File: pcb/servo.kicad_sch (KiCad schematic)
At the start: 1 part, among them J5 0436500315

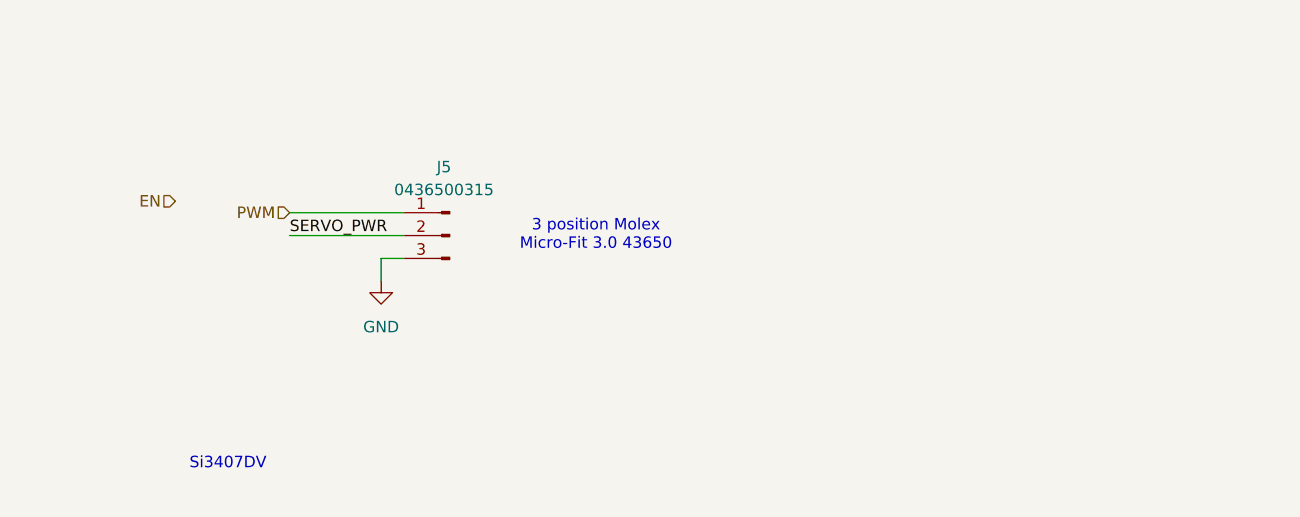
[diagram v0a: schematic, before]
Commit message: Create servo schematic
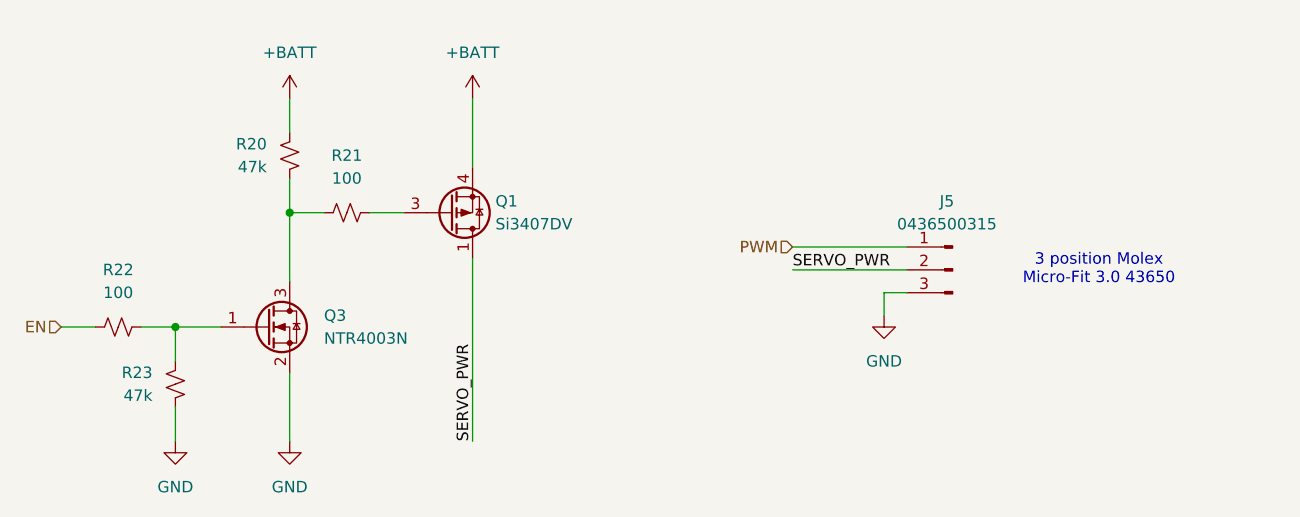
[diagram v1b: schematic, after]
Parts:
- added Q1: Si3407DV, Package_SO:TSOP-6_1.65x3.05mm_P0.95mm, symbol Vishay_FET:Si3407DV
- added Q3: NTR4003N, Package_TO_SOT_SMD:SOT-23-3, symbol Transistor_FET:Q_NMOS_GSD
- added R20, R23: 47k, symbol Device:R_Small_US
- added R21, R22: 100, symbol Device:R_Small_US
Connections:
- net EN: now also R22.1
- net GND: now also Q3.2 (S), R23.2
- net SERVO_PWR: now also Q1.1 (D), Q1.2 (D), Q1.5 (D), Q1.6 (D)
- new net: Q3.3 (D), R20.2, R21.1
- new net: Q1.3 (G), R21.2
- new net: Q3.1 (G), R22.2, R23.1
- new net +BATT: Q1.4 (S), R20.1
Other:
- note removed: "Si3407DV"
- moved on the sheet: J5

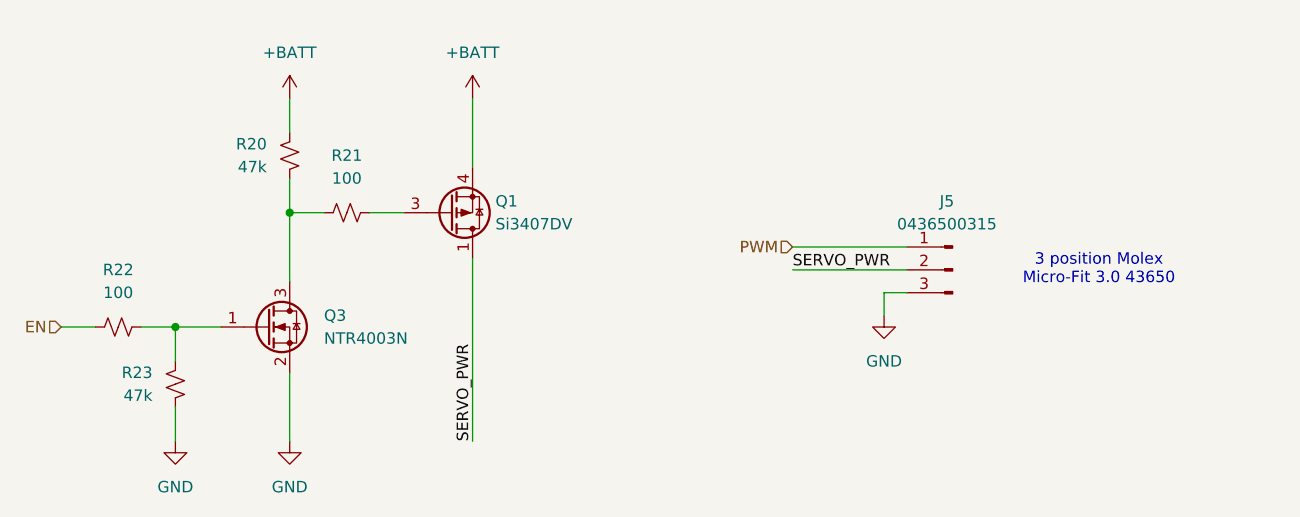
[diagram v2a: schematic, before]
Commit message: Update servo.kicad_sch
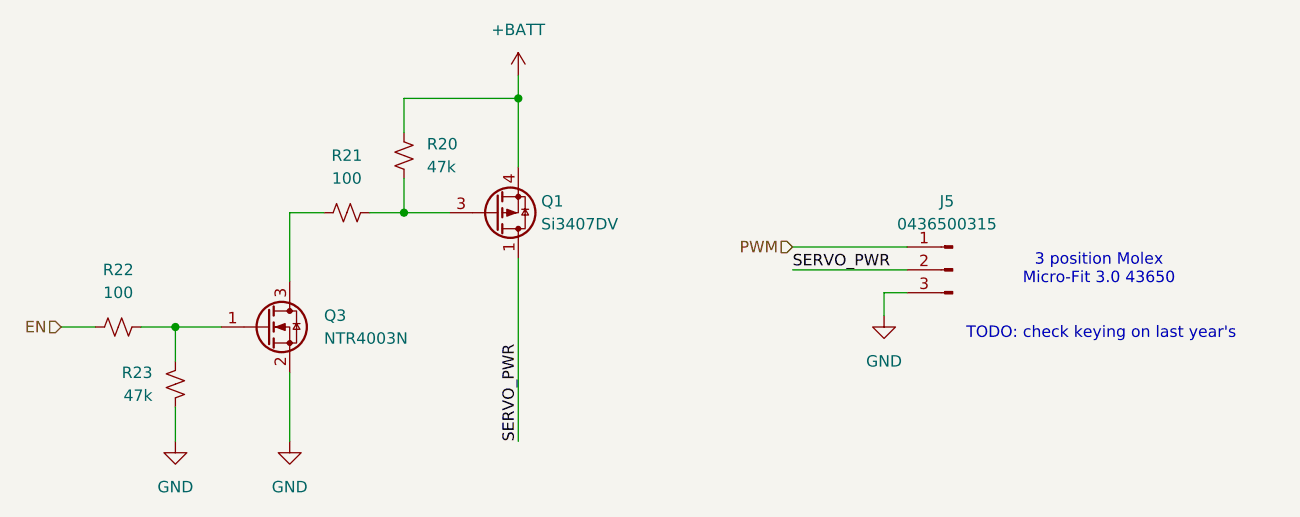
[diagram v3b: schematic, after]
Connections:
- net at Q3.3 (D), R21.1: no longer R20.2
- net at Q1.3 (G), R21.2: now also R20.2
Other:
- note added: "TODO: check keying on last year's"
- moved on the sheet: Q1, R20
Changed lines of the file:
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@@
 		)
 	)
-	(junction
-		(at 63.5 50.8)
-		(diameter 0)
-		(color 0 0 0 0)
+	(text "TODO: check keying on last year's"
+		(exclude_from_sim no)
+		(at 153.67 64.262 0)
+		(effects
+			(font
+				(size 1.27 1.27)
+			)
+		)
 	)
 	(junction
@@
 		(color 0 0 0 0)
 	)
+	(junction
+		(at 88.9 38.1)
+		(diameter 0)
+		(color 0 0 0 0)
+	)
+	(junction
+		(at 76.2 50.8)
+		(diameter 0)
+		(color 0 0 0 0)
+	)
 	(wire
 		(pts
@@
 	(wire
 		(pts
-			(xy 63.5 38.1) (xy 63.5 41.91)
+			(xy 88.9 38.1) (xy 88.9 45.72)
 		)
 		(stroke
@@
 	(wire
 		(pts
-			(xy 83.82 38.1) (xy 83.82 45.72)
+			(xy 76.2 50.8) (xy 81.28 50.8)
 		)
 		(stroke
@@
 	(wire
 		(pts
+			(xy 76.2 38.1) (xy 76.2 41.91)
+		)
+		(stroke
+			(width 0)
+			(type default)
+		)
+	)
+	(wire
+		(pts
 			(xy 129.54 59.69) (xy 132.08 59.69)
 		)
@@
 	(wire
 		(pts
+			(xy 76.2 38.1) (xy 88.9 38.1)
+		)
+		(stroke
+			(width 0)
+			(type default)
+		)
+	)
+	(wire
+		(pts
+			(xy 88.9 35.56) (xy 88.9 38.1)
+		)
+		(stroke
+			(width 0)
+			(type default)
+		)
+	)
+	(wire
+		(pts
 			(xy 63.5 50.8) (xy 67.31 50.8)
 		)
@@
 	(wire
 		(pts
-			(xy 63.5 46.99) (xy 63.5 50.8)
-		)
-		(stroke
-			(width 0)
-			(type default)
-		)
-	)
-	(wire
-		(pts
-			(xy 83.82 55.88) (xy 83.82 76.2)
+			(xy 76.2 46.99) (xy 76.2 50.8)
+		)
+		(stroke
+			(width 0)
+			(type default)
+		)
+	)
+	(wire
+		(pts
+			(xy 88.9 55.88) (xy 88.9 76.2)
 		)
 		(stroke
@@
 	)
 	(label "SERVO_PWR"
-		(at 83.82 76.2 90)
+		(at 88.9 76.2 90)
 		(effects
 			(font
@@
 	(symbol
 		(lib_id "Device:R_Small_US")
-		(at 63.5 44.45 0)
-		(mirror y)
+		(at 76.2 44.45 0)
 		(unit 1)
 		(exclude_from_sim no)
@@
 		(dnp no)
 		(property "Reference" "R20"
-			(at 60.96 43.1799 0)
+			(at 78.74 43.1799 0)
 			(effects
 				(font
@@
 		)
 		(property "Value" "47k"
-			(at 60.96 45.7199 0)
+			(at 78.74 45.7199 0)
 			(effects
 				(font
@@
 		)
 		(property "Footprint" ""
-			(at 63.5 44.45 0)
+			(at 76.2 44.45 0)
 			(effects
 				(font
@@
 		)
 		(property "Datasheet" "~"
-			(at 63.5 44.45 0)
+			(at 76.2 44.45 0)
 			(effects
 				(font
@@
 		)
 		(property "Description" "Resistor, small US symbol"
-			(at 63.5 44.45 0)
+			(at 76.2 44.45 0)
 			(effects
 				(font
@@
 	(symbol
 		(lib_id "power:+BATT")
-		(at 83.82 38.1 0)
+		(at 88.9 35.56 0)
 		(unit 1)
 		(exclude_from_sim no)
@@
 		(fields_autoplaced yes)
 		(property "Reference" "#PWR050"
-			(at 83.82 41.91 0)
+			(at 88.9 39.37 0)
 			(effects
 				(font
@@
 		)
 		(property "Value" "+BATT"
-			(at 83.82 33.02 0)
+			(at 88.9 30.48 0)
 			(effects
 				(font
@@
 		)
 		(property "Footprint" ""
-			(at 83.82 38.1 0)
+			(at 88.9 35.56 0)
 			(effects
 				(font
@@
 		)
 		(property "Datasheet" ""
-			(at 83.82 38.1 0)
+			(at 88.9 35.56 0)
 			(effects
 				(font
@@
 		)
 		(property "Description" "Power symbol creates a global label with name \"+BATT\""
-			(at 83.82 38.1 0)
+			(at 88.9 35.56 0)
 			(effects
 				(font
@@
 	(symbol
 		(lib_id "Vishay_FET:Si3407DV")
-		(at 81.28 50.8 0)
+		(at 86.36 50.8 0)
 		(unit 1)
 		(exclude_from_sim no)
@@
 		(dnp no)
 		(property "Reference" "Q1"
-			(at 86.36 49.53 0)
+			(at 91.44 49.53 0)
 			(effects
 				(font
@@
 		)
 		(property "Value" "Si3407DV"
-			(at 86.36 52.07 0)
+			(at 91.44 52.07 0)
 			(effects
 				(font
@@
 		)
 		(property "Footprint" "Package_SO:TSOP-6_1.65x3.05mm_P0.95mm"
-			(at 81.28 29.972 0)
+			(at 86.36 29.972 0)
 			(effects
 				(font
@@
 		)
 		(property "Datasheet" "https://www.vishay.com/docs/69987/si3407dv.pdf"
-			(at 81.28 29.972 0)
+			(at 86.36 29.972 0)
 			(effects
 				(font
@@
 		)
 		(property "Description" "P-Channel 20-V (D-S) MOSFET 24mOhm Rds(on) 8A Vishay Siliconix"
-			(at 81.28 29.972 0)
+			(at 86.36 29.972 0)
 			(effects
 				(font
@@
 					(unit 1)
 				)
-			)
-		)
-	)
-	(symbol
-		(lib_id "power:+BATT")
-		(at 63.5 38.1 0)
-		(unit 1)
-		(exclude_from_sim no)
-		(in_bom yes)
-		(on_board yes)
-		(dnp no)
-		(fields_autoplaced yes)
-		(property "Reference" "#PWR054"
-			(at 63.5 41.91 0)
-			(effects
-				(font
-					(size 1.27 1.27)
-				)
-				(hide yes)
-			)
-		)
-		(property "Value" "+BATT"
-			(at 63.5 33.02 0)
-			(effects
-				(font
-					(size 1.27 1.27)
-				)
-			)
-		)
-		(property "Footprint" ""
-			(at 63.5 38.1 0)
-			(effects
-				(font
-					(size 1.27 1.27)
-				)
-				(hide yes)
-			)
-		)
-		(property "Datasheet" ""
-			(at 63.5 38.1 0)
-			(effects
-				(font
-					(size 1.27 1.27)
-				)
-				(hide yes)
-			)
-		)
-		(property "Description" "Power symbol creates a global label with name \"+BATT\""
-			(at 63.5 38.1 0)
-			(effects
-				(font
-					(size 1.27 1.27)
-				)
-				(hide yes)
-			)
-		)
-		(pin "1"
-		)
-		(instances
-			(project "airbrake_mod"
-				(path "/1f4fd4ed-9886-4375-a5ac-dc32d5760936/27a1e4e9-ed52-4396-b65c-2ca15ccf5a1d"
-					(reference "#PWR054")
-					(unit 1)
-				)
